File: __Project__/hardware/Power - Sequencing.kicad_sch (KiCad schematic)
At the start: 0 parts

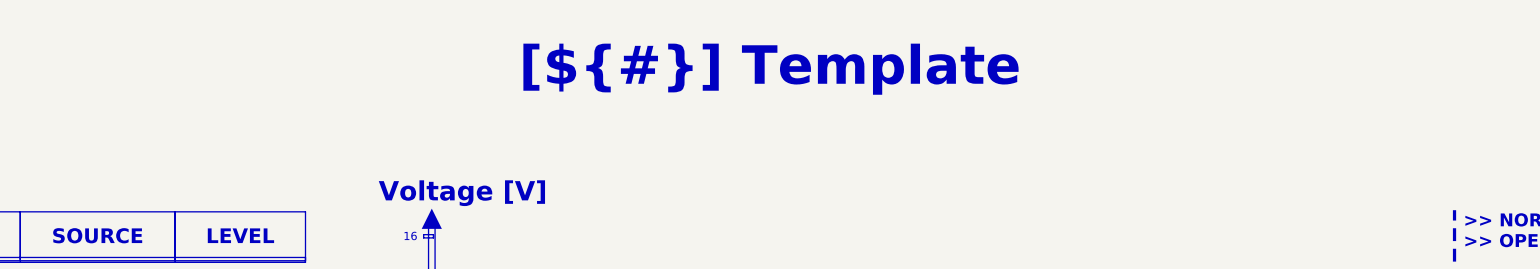
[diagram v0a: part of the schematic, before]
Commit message: Fix JST footprints
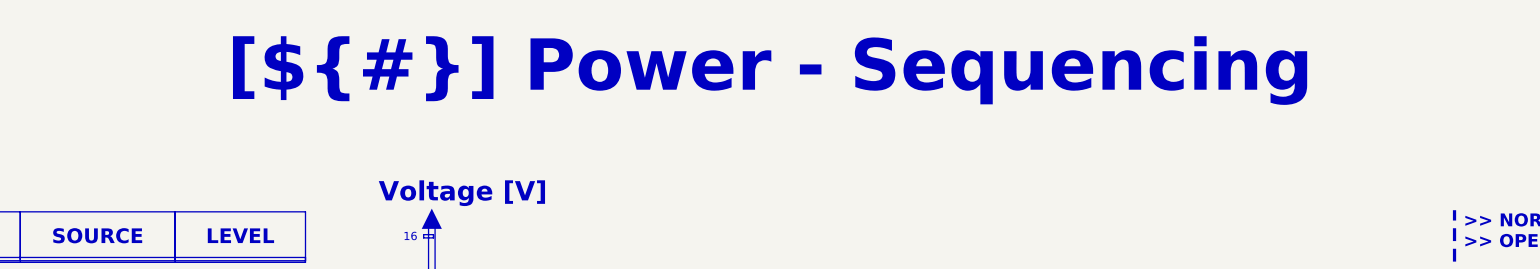
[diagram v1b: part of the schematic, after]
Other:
- title: Template -> Power - Sequencing
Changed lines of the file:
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@@
 	(paper "A4")
 	(title_block
-		(title "Template")
+		(title "Power - Sequencing")
 		(date "2025-06-05")
 		(rev "${REVISION}")
@@
 		)
 	)
+	(text_box "[${#}] ${TITLE}"
+		(exclude_from_sim no)
+		(at 12.7 12.7 0)
+		(size 271.78 20.32)
+		(margins 5.9999 5.9999 5.9999 5.9999)
+		(stroke
+			(width -0.0001)
+			(type default)
+		)
+		(fill
+			(type none)
+		)
+		(effects
+			(font
+				(face "Times New Roman")
+				(size 8 8)
+				(thickness 1.2)
+				(bold yes)
+				(color 162 22 34 1)
+			)
+		)
+	)
 	(text_box "26"
 		(exclude_from_sim no)
@@
 			)
 		)
-	)
-	(text_box "[${#}] ${TITLE}"
-		(exclude_from_sim no)
-		(at 80.01 16.51 0)
-		(size 137.16 12.7)
-		(margins 4.4999 4.4999 4.4999 4.4999)
-		(stroke
-			(width -0.0001)
-			(type default)
-		)
-		(fill
-			(type none)
-		)
-		(effects
-			(font
-				(face "Times New Roman")
-				(size 6 6)
-				(thickness 1.2)
-				(bold yes)
-				(color 162 22 34 1)
-			)
-		)
